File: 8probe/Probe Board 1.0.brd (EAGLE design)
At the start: 54 x 13 mm, 61 parts, among them Q3 2N7002, Q4 2N7002, U1 LTC2495CUHFPBF, U3 MAX6037AAUKADJ+T, U4 CSTCE16M0V53A-R0, U5 TPS79733DCKR, U6 ATMEGA328P_TQFPQFN_32

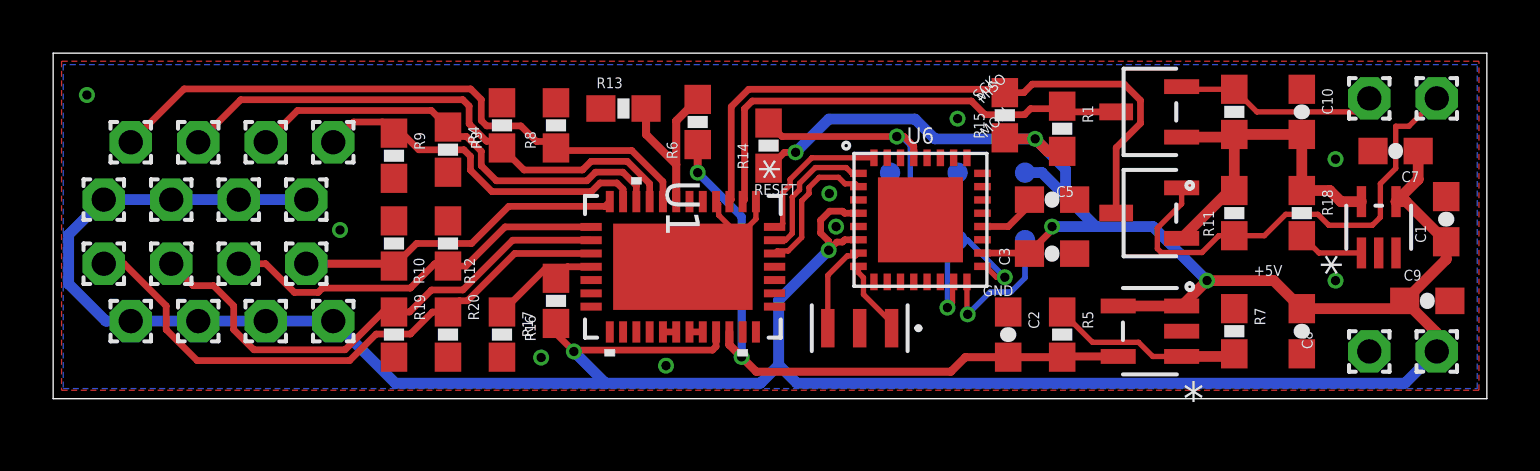
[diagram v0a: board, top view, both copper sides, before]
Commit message: Minor layout updates to 8probe
Split ground plane redistributed decoupling capacitors appropriately, moved input cable connections to be in a row, fixed package on Q1 and Q2, corrected ground pad on ATMEGA. Silk screen still needs updating
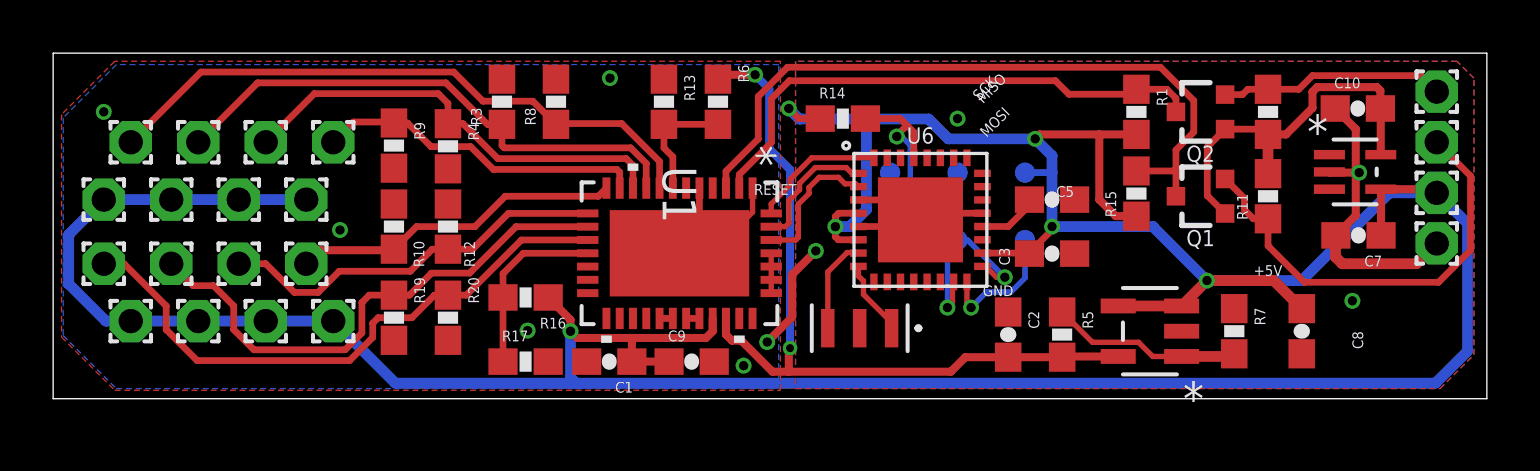
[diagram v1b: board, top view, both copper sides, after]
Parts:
- removed Q3, Q4: 2N7002, 2N7002(2):SOT23-3L
- removed R18: 30k, SparkFun:0603-RES
- added Q1, Q2: 2N7002, bschulz:SOT323
- moved C1 31.9 mm to (30.5, 1.40), turned to 180 degrees
- moved C9 27.8 mm to (33.6, 1.40)
- moved 5V 5.97 mm to (61.6, 7.75), turned to 180 degrees
- moved R15 5.76 mm to (50.3, 7.72)
- moved GND 4.79 mm to (61.6, 5.84), turned to 180 degrees
- moved C7 3.47 mm to (58.6, 6.15)
- moved R14 2.97 mm to (39.2, 10.5), turned to 0 degrees
- moved R1 2.87 mm to (50.3, 10.8)
- moved SCL3.3V 2.55 mm to (61.6, 11.6), turned to 180 degrees
- moved U5 2.26 mm to (58.5, 8.53), turned to 0 degrees
- moved C10 2.11 mm to (58.6, 10.9), turned to 0 degrees
- moved SDA3.3V 1.65 mm to (61.6, 9.65), turned to 180 degrees
- moved R13 1.55 mm to (32.5, 11.2), turned to 90 degrees
- moved R11 1.42 mm to (55.2, 7.62)
- moved R17 1.35 mm to (27.3, 1.40), turned to 0 degrees
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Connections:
- removed net N$9: R18.2, U5.1
- net 3.3V: now also Q1.1, Q2.1; no longer Q3.1, Q4.1, R18.1
- net COM: now also U6.EP
- net SCL3.3V: now also Q2.2; no longer Q3.2
- net SCL5V: now also Q2.3; no longer Q3.5
- net SDA3.3V: now also Q1.2; no longer Q4.2
- net SDA5V: now also Q1.3; no longer Q4.5
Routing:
- net COM: track 3.01 -> 30.2 mm, vias 9 -> 10
- net +5V: track 134.9 -> 147.2 mm
- net REF_V: track 24.5 -> 29.4 mm
- net RESET: track 10.8 -> 8.11 mm
- net N$9: track 2.51 -> 0.00 mm
- net SCL5V: track 18.1 -> 20.5 mm
- net SDA5V: track 24.3 -> 26.7 mm
- net VCC_READ: track 4.54 -> 6.82 mm
- net N$5: track 6.76 -> 4.57 mm
- net CH6: track 19.4 -> 20.6 mm
- net 3.3V: track 13.9 -> 15.0 mm
- net SDA3.3V: track 17.7 -> 16.8 mm
- net SCL3.3V: track 7.67 -> 8.51 mm
- net CH3: track 13.3 -> 12.5 mm
- net IO2: track 5.62 -> 5.06 mm
